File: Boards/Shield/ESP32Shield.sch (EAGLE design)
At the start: 27 parts, among them Q1 220mA/50V/3.5Ω, U1 5V

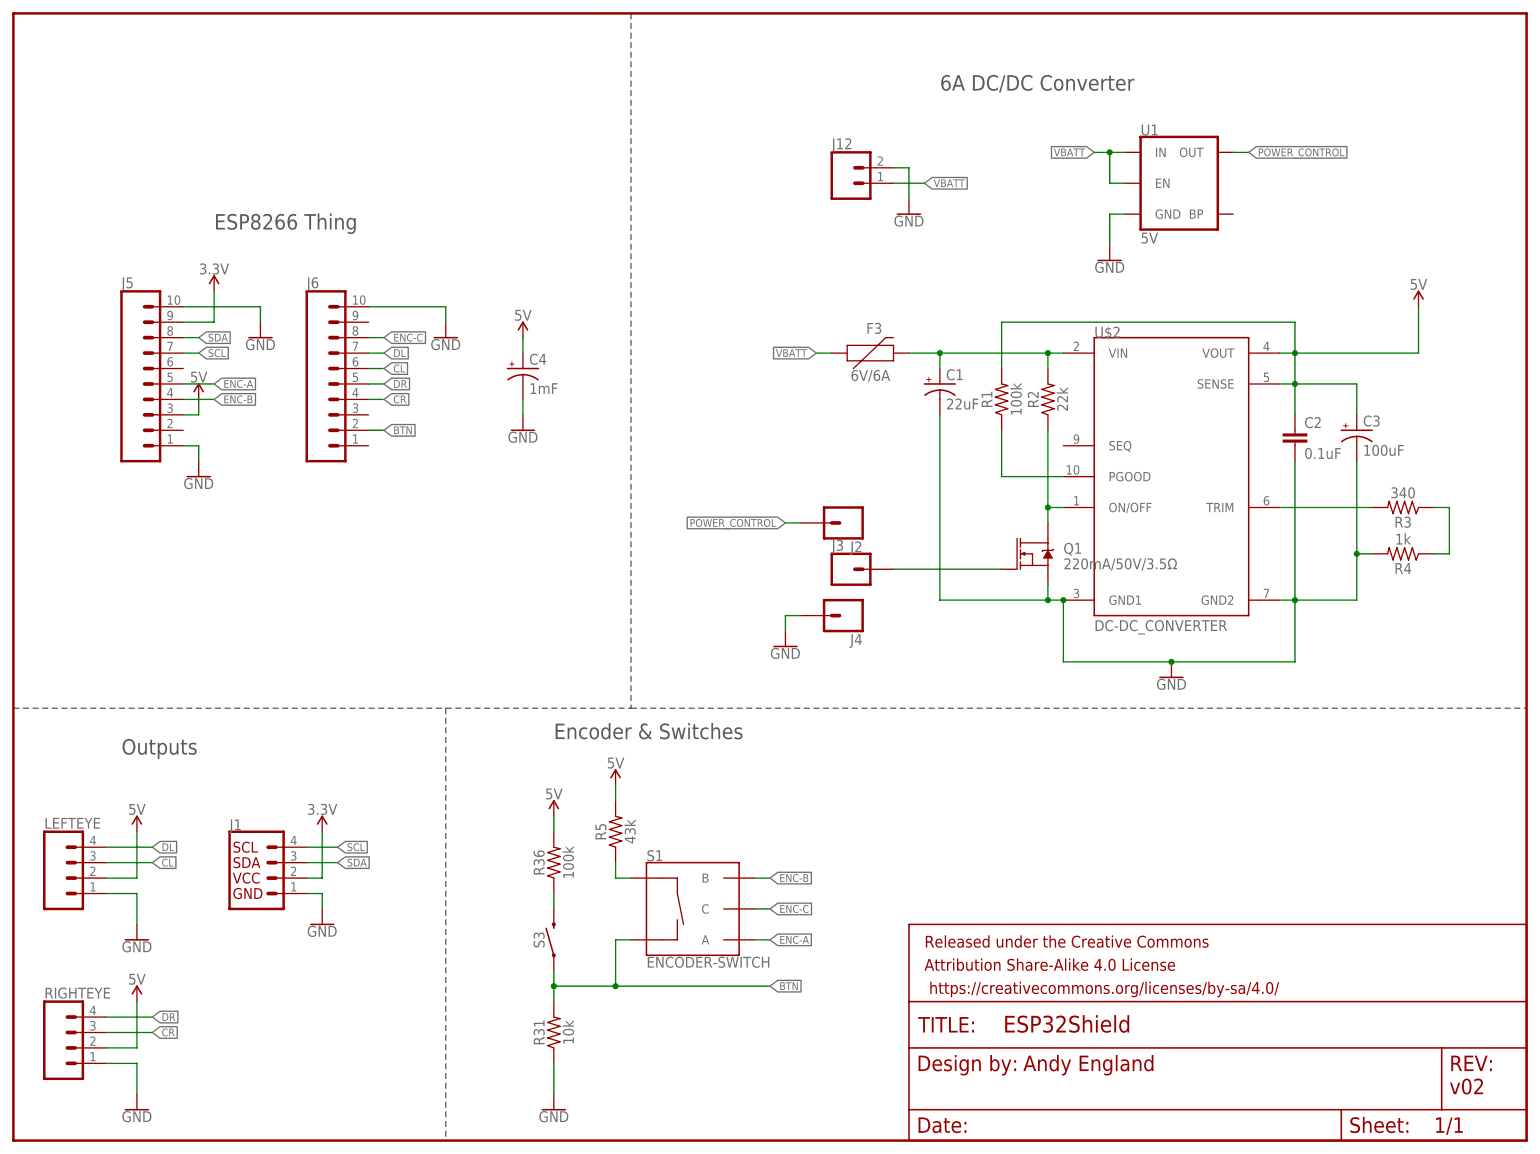
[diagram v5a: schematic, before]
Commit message: Updating interrupts, power structure
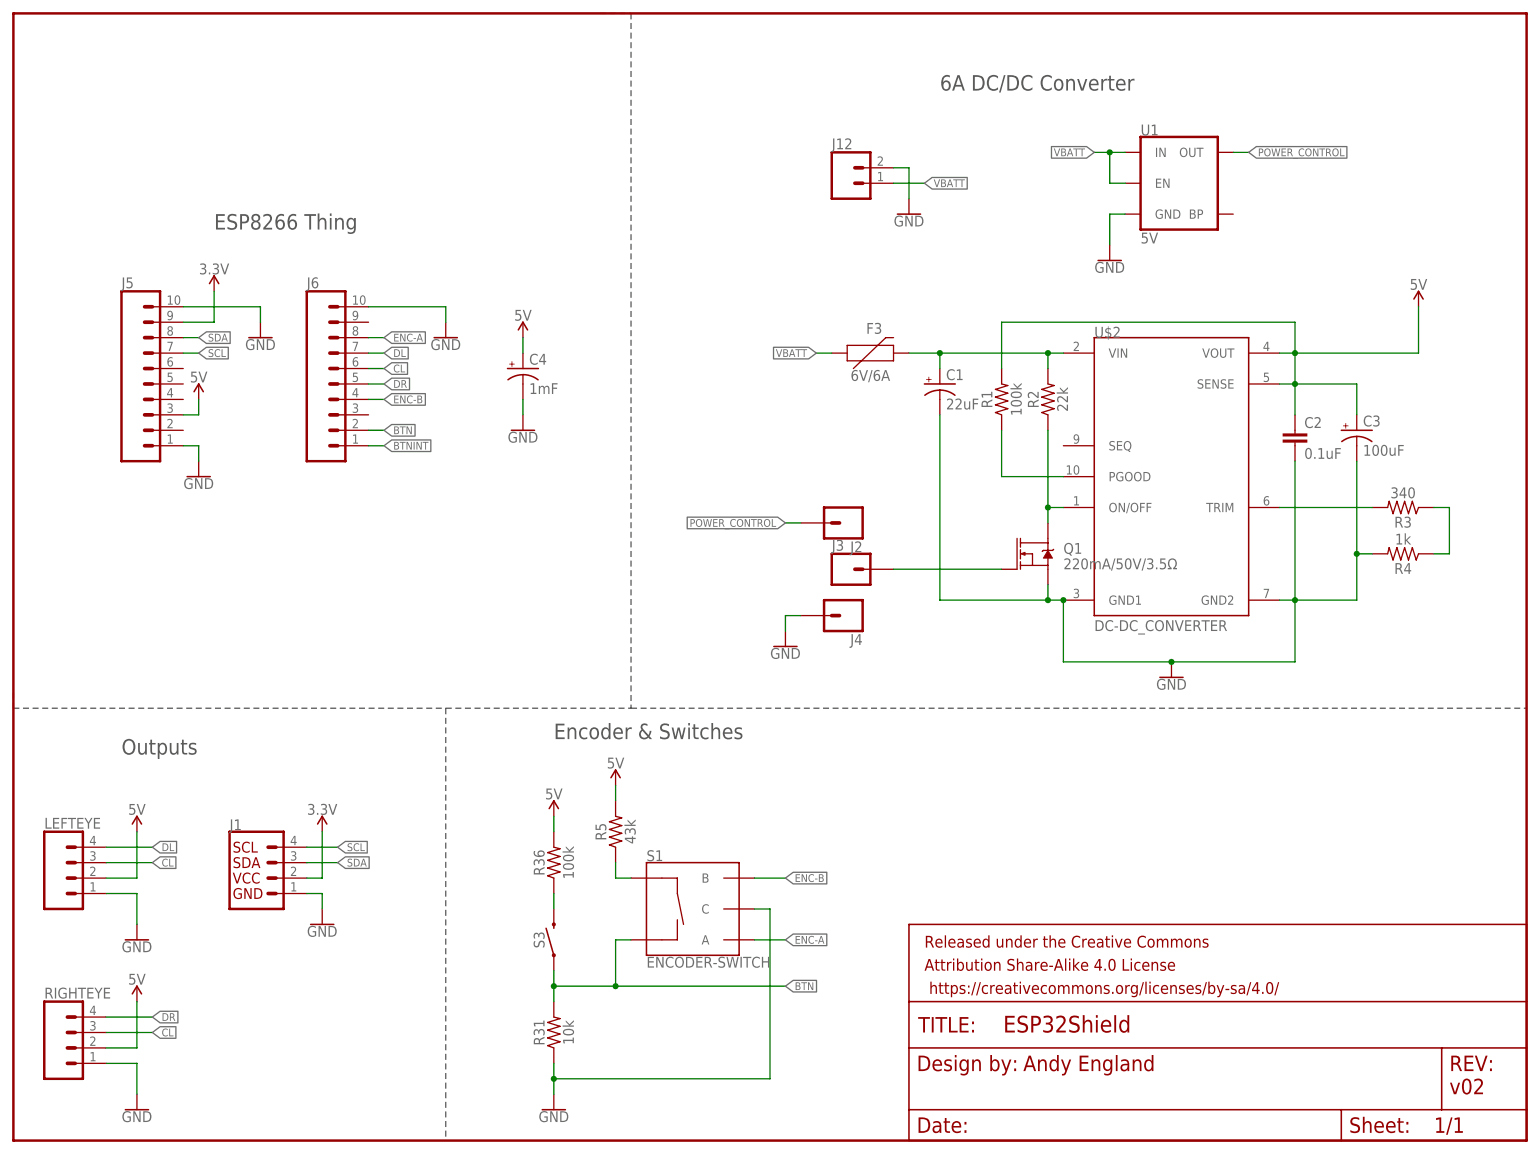
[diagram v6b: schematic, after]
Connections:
- removed net CR: J6.4, RIGHTEYE.3
- removed net ENC-C: J6.8, S1.C
- new net BTNINT: J6.1
- net CL: now also RIGHTEYE.3
- net ENC-A: now also J6.8; no longer J5.5
- net ENC-B: now also J6.4; no longer J5.4
- net GND: now also S1.C
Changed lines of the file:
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@@
 <pinref part="GND20" gate="1" pin="GND"/>
 <pinref part="R31" gate="G$1" pin="1"/>
-<wire x1="88.9" y1="7.62" x2="88.9" y2="12.7" width="0.1524" layer="91"/>
+<wire x1="88.9" y1="7.62" x2="88.9" y2="10.16" width="0.1524" layer="91"/>
+<pinref part="S1" gate="G$1" pin="C"/>
+<wire x1="88.9" y1="10.16" x2="88.9" y2="12.7" width="0.1524" layer="91"/>
+<wire x1="121.92" y1="38.1" x2="124.46" y2="38.1" width="0.1524" layer="91"/>
+<wire x1="124.46" y1="38.1" x2="124.46" y2="10.16" width="0.1524" layer="91"/>
+<wire x1="124.46" y1="10.16" x2="88.9" y2="10.16" width="0.1524" layer="91"/>
+<junction x="88.9" y="10.16"/>
 </segment>
 <segment>
@@
 <junction x="88.9" y="25.4"/>
 <wire x1="88.9" y1="25.4" x2="99.06" y2="25.4" width="0.1524" layer="91"/>
-<label x="124.46" y="25.4" size="1.27" layer="95" xref="yes"/>
+<label x="127" y="25.4" size="1.27" layer="95" xref="yes"/>
 <pinref part="S3" gate="G$1" pin="1"/>
 <pinref part="S1" gate="G$1" pin="SW-"/>
-<wire x1="99.06" y1="25.4" x2="124.46" y2="25.4" width="0.1524" layer="91"/>
+<wire x1="99.06" y1="25.4" x2="127" y2="25.4" width="0.1524" layer="91"/>
 <wire x1="101.6" y1="33.02" x2="99.06" y2="33.02" width="0.1524" layer="91"/>
 <wire x1="99.06" y1="33.02" x2="99.06" y2="25.4" width="0.1524" layer="91"/>
@@
 <label x="60.96" y="127" size="1.27" layer="95" xref="yes"/>
 </segment>
+<segment>
+<pinref part="RIGHTEYE" gate="G$1" pin="3"/>
+<wire x1="15.24" y1="17.78" x2="22.86" y2="17.78" width="0.1524" layer="91"/>
+<label x="22.86" y="17.78" size="1.27" layer="95" xref="yes"/>
+</segment>
 </net>
 <net name="DR" class="0">
@@
 </segment>
 </net>
-<net name="CR" class="0">
-<segment>
-<pinref part="RIGHTEYE" gate="G$1" pin="3"/>
-<wire x1="15.24" y1="17.78" x2="22.86" y2="17.78" width="0.1524" layer="91"/>
-<label x="22.86" y="17.78" size="1.27" layer="95" font="vector" xref="yes"/>
+<net name="ENC-A" class="0">
+<segment>
+<pinref part="S1" gate="G$1" pin="A"/>
+<wire x1="121.92" y1="33.02" x2="127" y2="33.02" width="0.1524" layer="91"/>
+<label x="127" y="33.02" size="1.27" layer="95" font="vector" xref="yes"/>
+</segment>
+<segment>
+<pinref part="J6" gate="G$1" pin="8"/>
+<wire x1="58.42" y1="132.08" x2="60.96" y2="132.08" width="0.1524" layer="91"/>
+<label x="60.96" y="132.08" size="1.27" layer="95" xref="yes"/>
+</segment>
+</net>
+<net name="ENC-B" class="0">
+<segment>
+<pinref part="S1" gate="G$1" pin="B"/>
+<wire x1="121.92" y1="43.18" x2="127" y2="43.18" width="0.1524" layer="91"/>
+<label x="127" y="43.18" size="1.27" layer="95" font="vector" xref="yes"/>
 </segment>
 <segment>
@@
 <wire x1="58.42" y1="121.92" x2="60.96" y2="121.92" width="0.1524" layer="91"/>
 <label x="60.96" y="121.92" size="1.27" layer="95" xref="yes"/>
-</segment>
-</net>
-<net name="ENC-A" class="0">
-<segment>
-<pinref part="S1" gate="G$1" pin="A"/>
-<wire x1="121.92" y1="33.02" x2="124.46" y2="33.02" width="0.1524" layer="91"/>
-<label x="124.46" y="33.02" size="1.27" layer="95" font="vector" xref="yes"/>
-</segment>
-<segment>
-<pinref part="J5" gate="G$1" pin="5"/>
-<wire x1="27.94" y1="124.46" x2="33.02" y2="124.46" width="0.1524" layer="91"/>
-<label x="33.02" y="124.46" size="1.27" layer="95" xref="yes"/>
-</segment>
-</net>
-<net name="ENC-C" class="0">
-<segment>
-<pinref part="S1" gate="G$1" pin="C"/>
-<wire x1="121.92" y1="38.1" x2="124.46" y2="38.1" width="0.1524" layer="91"/>
-<label x="124.46" y="38.1" size="1.27" layer="95" font="vector" xref="yes"/>
-</segment>
-<segment>
-<pinref part="J6" gate="G$1" pin="8"/>
-<wire x1="58.42" y1="132.08" x2="60.96" y2="132.08" width="0.1524" layer="91"/>
-<label x="60.96" y="132.08" size="1.27" layer="95" xref="yes"/>
-</segment>
-</net>
-<net name="ENC-B" class="0">
-<segment>
-<pinref part="S1" gate="G$1" pin="B"/>
-<wire x1="121.92" y1="43.18" x2="124.46" y2="43.18" width="0.1524" layer="91"/>
-<label x="124.46" y="43.18" size="1.27" layer="95" font="vector" xref="yes"/>
-</segment>
-<segment>
-<pinref part="J5" gate="G$1" pin="4"/>
-<wire x1="33.02" y1="121.92" x2="27.94" y2="121.92" width="0.1524" layer="91"/>
-<label x="33.02" y="121.92" size="1.27" layer="95" xref="yes"/>
 </segment>
 </net>
@@
 </segment>
 </net>
+<net name="BTNINT" class="0">
+<segment>
+<pinref part="J6" gate="G$1" pin="1"/>
+<wire x1="58.42" y1="114.3" x2="60.96" y2="114.3" width="0.1524" layer="91"/>
+<label x="60.96" y="114.3" size="1.27" layer="95" xref="yes"/>
+</segment>
+</net>

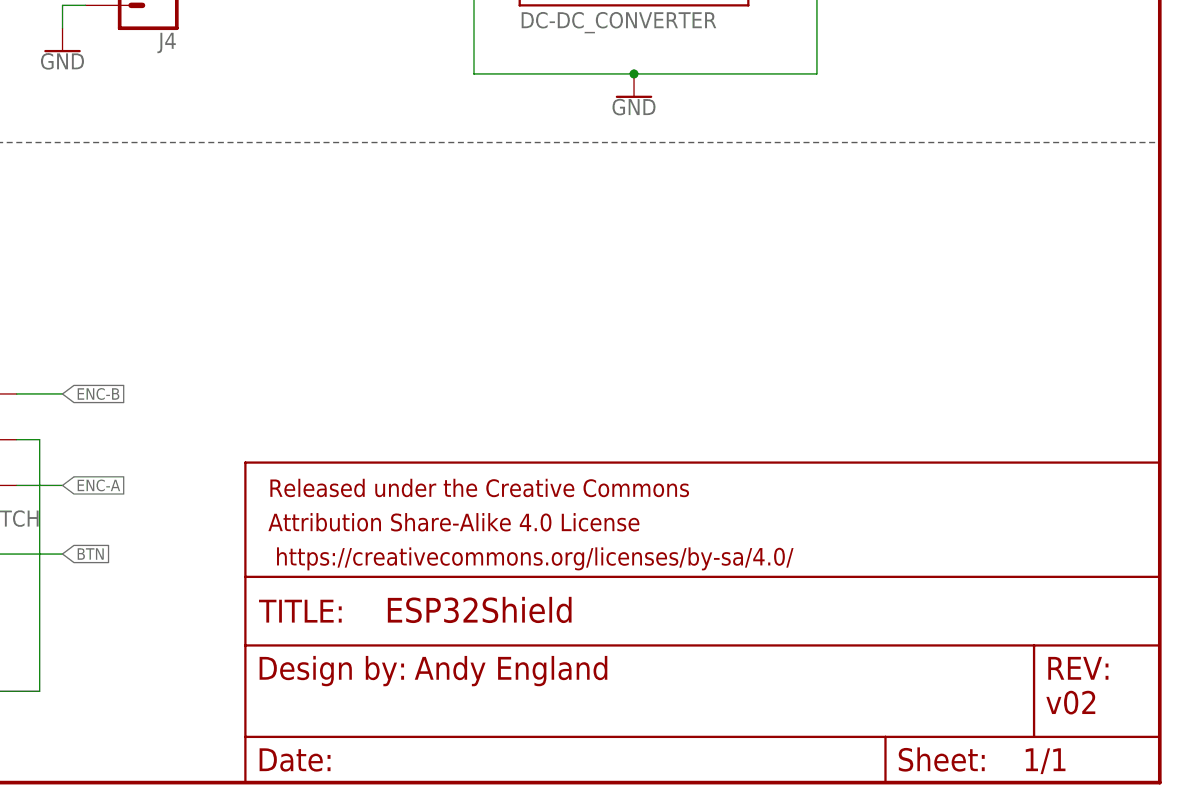
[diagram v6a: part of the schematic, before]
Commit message: adding new ESP8266Thing shield gerber
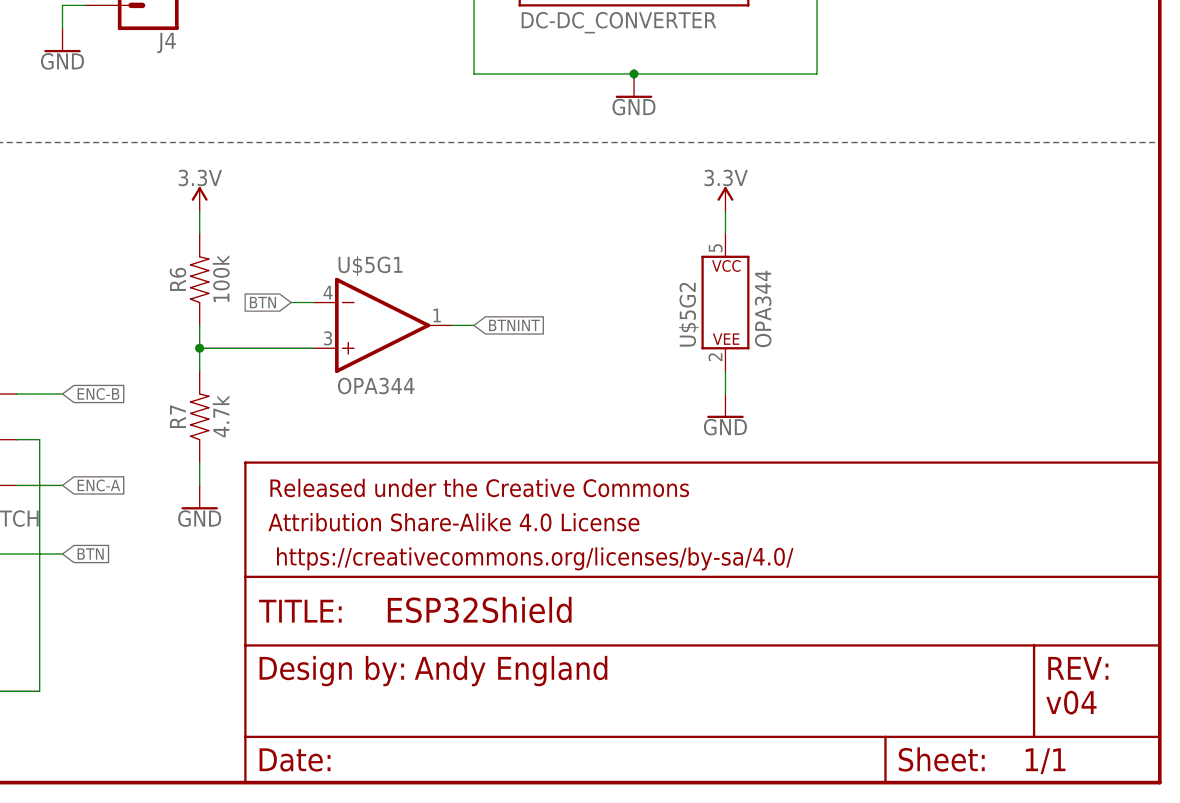
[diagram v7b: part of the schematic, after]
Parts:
- added R6: 100k, SparkFun-Resistors:100KOHM-0603-1/10W-1%
- added R7: 4.7k, SparkFun-Resistors:4.7KOHM-0603-1/10W-1%
- added U$5: OPA344, SparkFun-IC-Amplifiers:OPA344
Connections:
- new net N$9: R6.1, R7.2, U$5G1.+IN
- net 3.3V: now also R6.2, U$5G2.P$V+
- net BTN: now also U$5G1.-IN
- net BTNINT: now also U$5G1.OUT
- net GND: now also R7.1, U$5G2.P$V-
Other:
- note added: "v04"
- note removed: "v02"
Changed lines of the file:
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@@
 <?xml version="1.0" encoding="utf-8"?>
 <!DOCTYPE eagle SYSTEM "eagle.dtd">
-<eagle version="7.7.0">
+<eagle version="9.0.1">
 <drawing>
 <settings>
 <setting alwaysvectorfont="no"/>
+<setting keepoldvectorfont="yes"/>
 <setting verticaltext="up"/>
 </settings>
@@
 <part name="GND9" library="SparkFun-PowerSymbols" deviceset="GND" device=""/>
 <part name="R5" library="SparkFun-Resistors" deviceset="43KOHM" device="-0603-1/10W-1%" value="43k"/>
+<part name="U$5" library="SparkFun-IC-Amplifiers" deviceset="OPA344" device="" value="OPA344"/>
+<part name="GND3" library="SparkFun-PowerSymbols" deviceset="GND" device=""/>
+<part name="SUPPLY6" library="SparkFun-PowerSymbols" deviceset="3.3V" device=""/>
+<part name="R6" library="SparkFun-Resistors" deviceset="100KOHM" device="-0603-1/10W-1%" value="100k"/>
+<part name="R7" library="SparkFun-Resistors" deviceset="4.7KOHM" device="-0603-1/10W-1%" value="4.7k"/>
+<part name="SUPPLY7" library="SparkFun-PowerSymbols" deviceset="3.3V" device=""/>
+<part name="GND10" library="SparkFun-PowerSymbols" deviceset="GND" device=""/>
 </parts>
 <sheets>
@@
 <text x="17.78" y="63.5" size="2.54" layer="97" font="vector">Outputs</text>
 <text x="166.116" y="11.43" size="2.54" layer="94" font="vector">Andy England</text>
-<text x="236.22" y="7.62" size="2.54" layer="94" font="vector">v02</text>
+<text x="236.22" y="7.62" size="2.54" layer="94" font="vector">v04</text>
 </plain>
 <instances>
@@
 <instance part="GND9" gate="1" x="71.12" y="132.08"/>
 <instance part="R5" gate="G$1" x="99.06" y="50.8" rot="R90"/>
+<instance part="U$5" gate="G1" x="162.56" y="50.8"/>
+<instance part="U$5" gate="G2" x="200.66" y="53.34"/>
+<instance part="GND3" gate="1" x="200.66" y="40.64"/>
+<instance part="SUPPLY6" gate="G$1" x="200.66" y="63.5"/>
+<instance part="R6" gate="G$1" x="142.24" y="55.88" rot="R90"/>
+<instance part="R7" gate="G$1" x="142.24" y="40.64" rot="R90"/>
+<instance part="SUPPLY7" gate="G$1" x="142.24" y="63.5"/>
+<instance part="GND10" gate="1" x="142.24" y="30.48"/>
 </instances>
 <busses>
@@
 <wire x1="71.12" y1="137.16" x2="71.12" y2="134.62" width="0.1524" layer="91"/>
 </segment>
+<segment>
+<pinref part="U$5" gate="G2" pin="P$V-"/>
+<pinref part="GND3" gate="1" pin="GND"/>
+<wire x1="200.66" y1="43.18" x2="200.66" y2="45.72" width="0.1524" layer="91"/>
+</segment>
+<segment>
+<pinref part="R7" gate="G$1" pin="1"/>
+<pinref part="GND10" gate="1" pin="GND"/>
+<wire x1="142.24" y1="33.02" x2="142.24" y2="35.56" width="0.1524" layer="91"/>
+</segment>
 </net>
 <net name="BTN" class="0">
@@
 <wire x1="58.42" y1="116.84" x2="60.96" y2="116.84" width="0.1524" layer="91"/>
 <label x="60.96" y="116.84" size="1.27" layer="95" xref="yes"/>
+</segment>
+<segment>
+<pinref part="U$5" gate="G1" pin="-IN"/>
+<wire x1="154.94" y1="53.34" x2="152.4" y2="53.34" width="0.1524" layer="91"/>
+<label x="152.4" y="53.34" size="1.27" layer="95" rot="R180" xref="yes"/>
 </segment>
 </net>
@@
 <wire x1="33.02" y1="134.62" x2="33.02" y2="139.7" width="0.1524" layer="91"/>
 </segment>
+<segment>
+<pinref part="U$5" gate="G2" pin="P$V+"/>
+<pinref part="SUPPLY6" gate="G$1" pin="3.3V"/>
+<wire x1="200.66" y1="63.5" x2="200.66" y2="60.96" width="0.1524" layer="91"/>
+</segment>
+<segment>
+<pinref part="R6" gate="G$1" pin="2"/>
+<pinref part="SUPPLY7" gate="G$1" pin="3.3V"/>
+<wire x1="142.24" y1="63.5" x2="142.24" y2="60.96" width="0.1524" layer="91"/>
+</segment>
 </net>
 <net name="DL" class="0">
@@
 <label x="60.96" y="114.3" size="1.27" layer="95" xref="yes"/>
 </segment>
-</net>
+<segment>
+<pinref part="U$5" gate="G1" pin="OUT"/>
+<wire x1="170.18" y1="50.8" x2="172.72" y2="50.8" width="0.1524" layer="91"/>
+<label x="172.72" y="50.8" size="1.27" layer="95" xref="yes"/>
+</segment>
+</net>
+<net name="N$9" class="0">
+<segment>
+<pinref part="U$5" gate="G1" pin="+IN"/>
+<pinref part="R6" gate="G$1" pin="1"/>
+<wire x1="142.24" y1="48.26" x2="154.94" y2="48.26" width="0.1524" layer="91"/>
+<wire x1="142.24" y1="50.8" x2="142.24" y2="48.26" width="0.1524" layer="91"/>
+<junction x="142.24" y="48.26"/>
+<pinref part="R7" gate="G$1" pin="2"/>
+<wire x1="142.24" y1="45.72" x2="142.24" y2="48.26" width="0.1524" layer="91"/>
+</segment>
+</net>
